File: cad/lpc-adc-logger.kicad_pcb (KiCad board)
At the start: 2 copper layers, 72 x 47 mm, 26 parts, among them J1 SD CARD, J3 SWD, J4 ANALOG IN

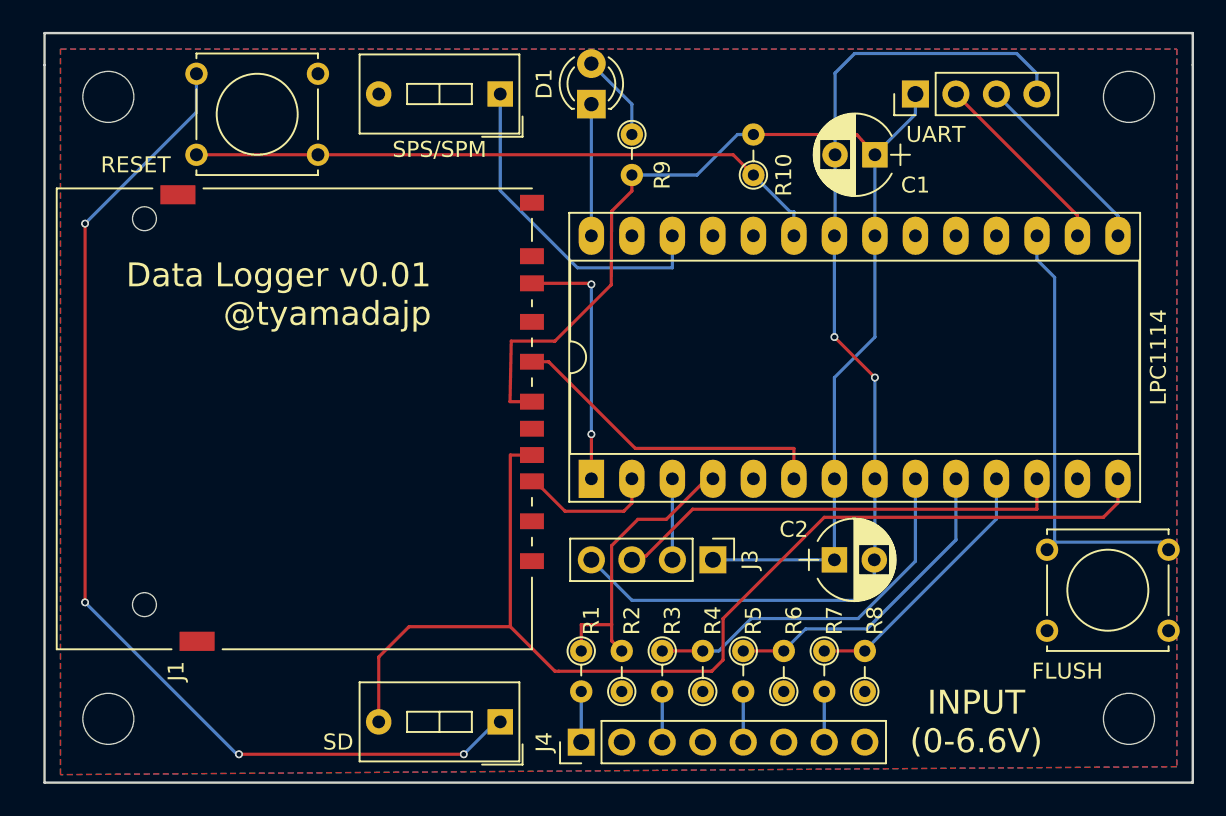
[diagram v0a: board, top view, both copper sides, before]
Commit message: - Fixed SD card MMC-CS pin - Added GPIO header - Added I2C header
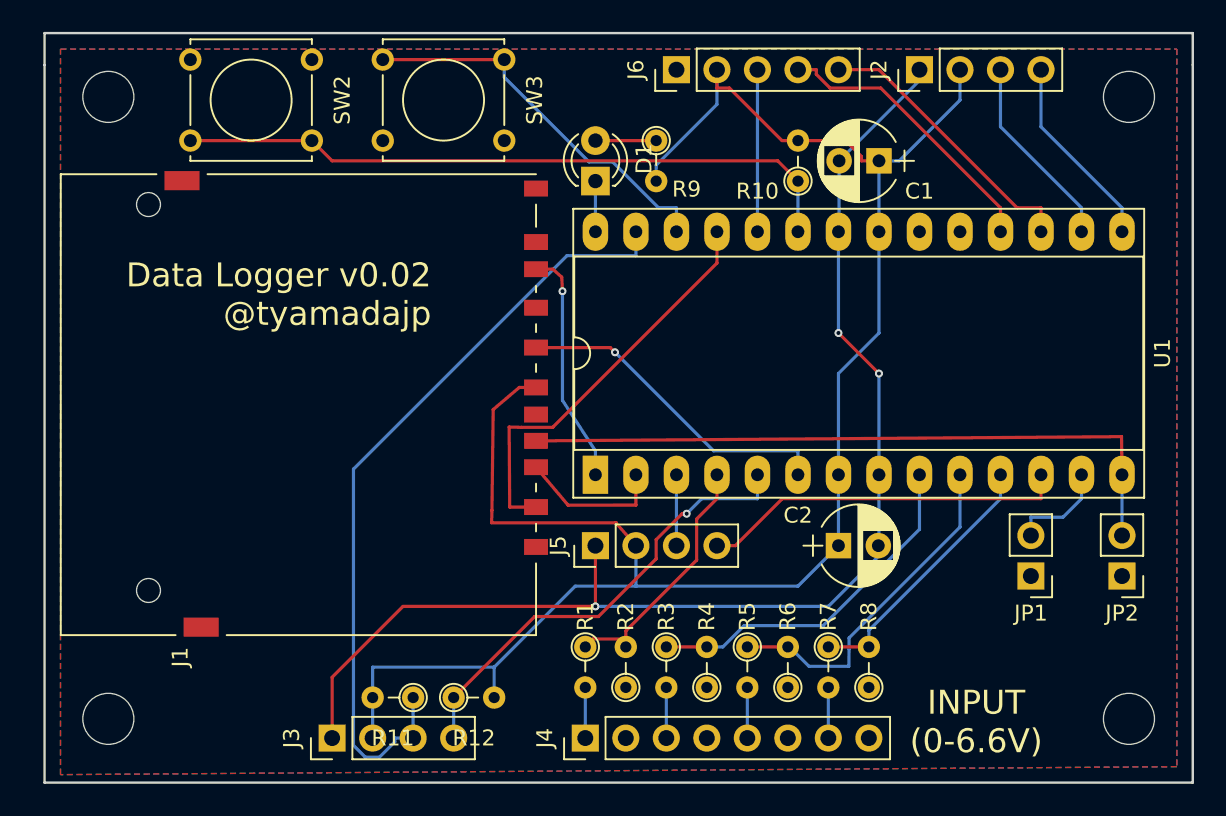
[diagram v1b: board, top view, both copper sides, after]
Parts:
- removed SD: SD_DETECT, Buttons_Switches_THT:SW_DIP_x1_W7.62mm_Slide
- removed SPS/SPM: SPS/SPM, Buttons_Switches_THT:SW_DIP_x1_W7.62mm_Slide
- removed UART: UART, Pin_Headers:Pin_Header_Straight_1x04_Pitch2.54mm
- added J2: UART, Pin_Headers:Pin_Header_Straight_1x04_Pitch2.54mm, F.Cu at (103.0, 115.4)
- added J5: SWD, Pin_Headers:Pin_Header_Straight_1x04_Pitch2.54mm, F.Cu at (82.7, 145.2)
- added J6: GPIO, Pin_Headers:Pin_Header_Straight_1x05_Pitch2.54mm, F.Cu at (87.8, 115.4)
- added JP1: RATE, Pin_Headers:Pin_Header_Straight_1x02_Pitch2.54mm, F.Cu at (110.0, 147.1)
- added JP2: SD, Pin_Headers:Pin_Header_Straight_1x02_Pitch2.54mm, F.Cu at (115.7, 147.1)
- added R11: 4.7K, Resistors_THT:R_Axial_DIN0204_L3.6mm_D1.6mm_P2.54mm_Vertical, F.Cu at (71.3, 154.8)
- added R12: 4.7K, Resistors_THT:R_Axial_DIN0204_L3.6mm_D1.6mm_P2.54mm_Vertical, F.Cu at (73.8, 154.8)
- J1: value SD CARD -> SD_CARD
- J3: value SWD -> I2C
- moved SW3 51.8 mm to (69.4, 114.8)
- moved J3 26.4 mm to (66.2, 157.3), turned to 90 degrees
- moved D1 4.83 mm to (82.7, 122.4)
- moved R10 2.82 mm to (95.4, 122.4)
- moved R9 1.57 mm to (86.5, 119.8)
- moved SW2 0.97 mm to (64.9, 119.8)
- moved J1 0.92 mm to (66.8, 136.4)
- moved C2 0.92 mm to (98.0, 145.2)
- moved C1 0.46 mm to (100.5, 121.1)
- moved U1 0.36 mm to (82.7, 140.8)
- moved J4 0.36 mm to (82.1, 157.3)
- moved R1 0.36 mm to (82.1, 151.6)
- moved R2 0.36 mm to (84.6, 154.1)
- moved R4 0.36 mm to (89.7, 154.1)
- moved R6 0.36 mm to (94.8, 154.1)
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- renumbered R5 to R2, R2 to R3, R6 to R4, R3 to R5, R7 to R6, R4 to R7, RESET to SW2, FLUSH to SW3, LPC1114 to U1
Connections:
- J1 pad 11: Net-(J1-Pad11) -> (no net)
- J1 pad 12: Net-(J1-Pad12) -> (no net)
- J1 pad 13: Net-(J1-Pad13) -> (no net)
- J1 pad 8: Net-(J1-Pad8) -> (no net)
- J1 pad 9: Net-(J1-Pad9) -> (no net)
- J3 pad 1: VCC -> GND
- J3 pad 2: Net-(J3-Pad2) -> VCC
- J3 pad 4: GND -> Net-(J3-Pad4)
- U1 pad 12: Net-(J3-Pad3) -> Net-(J5-Pad4)
- U1 pad 17: Net-(SW3-Pad1) -> Net-(J6-Pad5)
- U1 pad 19: Net-(U1-Pad19) -> (no net)
- U1 pad 20: Net-(U1-Pad20) -> (no net)
- U1 pad 25: Net-(U1-Pad25) -> Net-(J1-Pad1)
- U1 pad 26: Net-(SW1-Pad1) -> Net-(SW3-Pad1)
- U1 pad 27: Net-(U1-Pad27) -> Net-(J3-Pad3)
- U1 pad 3: Net-(J3-Pad2) -> Net-(J5-Pad3)
- U1 pad 5: Net-(U1-Pad5) -> Net-(J3-Pad4)
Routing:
- net GND: track 134.1 -> 78.8 mm, vias 6 -> 5
- net VCC: track 76.1 -> 117.6 mm
- net Net-(J1-Pad10): track 71.9 -> 42.9 mm
- net Net-(J3-Pad4): track 0.00 -> 29.0 mm, vias 0 -> 1
- net Net-(J1-Pad1): track 0.00 -> 25.9 mm
- net Net-(J5-Pad4): track 0.00 -> 23.0 mm
- net Net-(SW1-Pad1): track 20.9 -> 0.00 mm
- net Net-(J3-Pad3): track 28.6 -> 49.3 mm
- net Net-(J6-Pad4): track 0.00 -> 18.0 mm
- net Net-(J6-Pad5): track 0.00 -> 17.8 mm
- net Net-(J6-Pad3): track 0.00 -> 10.2 mm
- net Net-(JP1-Pad2): track 0.00 -> 6.31 mm
- net Net-(D1-Pad1): track 8.25 -> 3.17 mm
- net Net-(J3-Pad2): track 5.08 -> 0.00 mm
- net Net-(J5-Pad3): track 0.00 -> 4.45 mm
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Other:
- board text added: "Data Logger v0.02 @tyamadajp"
- board text removed: "Data Logger v0.01 @tyamadajp"

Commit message: [WIP] Added SPI header.
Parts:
- added J7: SPI, Pin_Headers:Pin_Header_Straight_1x06_Pitch2.54mm, F.Cu at (61.6, 157.3)
- JP2: value SD -> CARD
- moved J3 46.5 mm to (112.4, 151.7), turned to 270 degrees
- moved R11 38.8 mm to (109.6, 148.5), turned to 0 degrees
- moved R12 33.8 mm to (107.0, 148.5), turned to 180 degrees
- moved JP1 5.89 mm to (104.8, 144.4), turned to 90 degrees
- moved JP2 3.80 mm to (113.1, 144.4), turned to 90 degrees
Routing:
- net Net-(J3-Pad3): track 49.3 -> 0.00 mm
- net Net-(J3-Pad4): track 29.0 -> 0.00 mm, vias 1 -> 0
- net VCC: track 117.6 -> 92.6 mm
- net GND: track 78.8 -> 56.6 mm, vias 5 -> 4
- net Net-(R3-Pad1): track 22.4 -> 2.54 mm
- net Net-(R5-Pad1): track 21.6 -> 2.54 mm
- net Net-(R7-Pad1): track 16.8 -> 2.54 mm
- net Net-(JP1-Pad2): track 6.31 -> 0.00 mm
- net Net-(J1-Pad10): track 42.9 -> 39.1 mm
- net Net-(J1-Pad7): vias 1 -> 2
